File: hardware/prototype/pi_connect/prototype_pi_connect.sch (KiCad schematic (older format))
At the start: 29 parts, among them CON1 BARREL_JACK, SW1 Switch_SPDT_x2, SW2 Switch_SPDT_x2, U1 MCP23017, U2 Pi2_Connector, U3 MAX7221, U4 MAX7221

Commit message: Assign footprints
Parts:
- removed SW1, SW2: Switch_SPDT_x2, symbol Switch_SPDT_x2
- added SW1, SW2, SW3, SW4: SWITCH_INV, Buttons_Switches_ThroughHole:SW_Micro_SPST, symbol SWITCH_INV
- C1, C3: footprint (none) -> Discret:CP5
- C2, C4: footprint (none) -> Capacitors_ThroughHole:C_Disc_D6_P5
- CON1: footprint (none) -> Connect:BARREL_JACK
- D1, D10, D11, D12, D13, D14, D15, D16, D2, D3, D4, D5, D6, D7, D8, D9: footprint (none) -> LEDs:LED-5MM
- R1, R2: footprint (none) -> Resistors_ThroughHole:Resistor_Horizontal_RM10mm
- U1: footprint MODULE -> DIL28:DIL28
- U2: footprint MODULE -> CONN_02x20:CONN_02x20
- U3, U4: footprint MODULE -> DIL24:DIL24
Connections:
- net A_GPB0: now also SW4.3
- net A_GPB1: now also SW4.1
- net A_GPB2: now also SW3.3
- net A_GPB3: now also SW3.1
- net A_GPB4: now also SW2.3
- net A_GPB5: now also SW2.1
- net A_GPB6: now also SW1.3
- net A_GPB7: now also SW1.1
- net GND: now also SW1.2, SW2.2, SW3.2, SW4.2
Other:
- moved on the sheet: D1, D10, D11, D12, D13, D14, D15, D16, D2, D3, D4, D5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

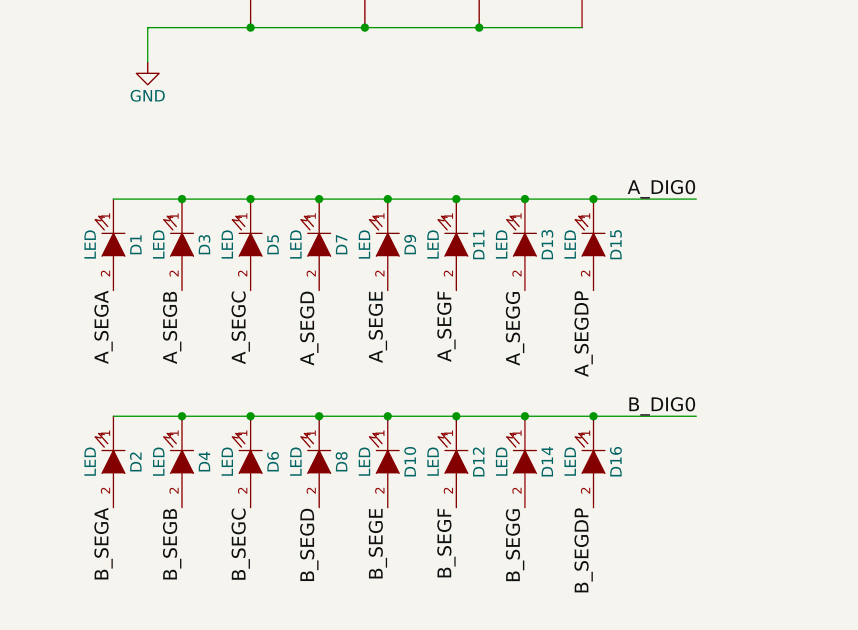
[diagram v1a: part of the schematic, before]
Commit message: Add footprint fot SPDT switches according to datasheet for 100SP4T1B1M2QEH. Also attempted to route some of this complex circuit manually.
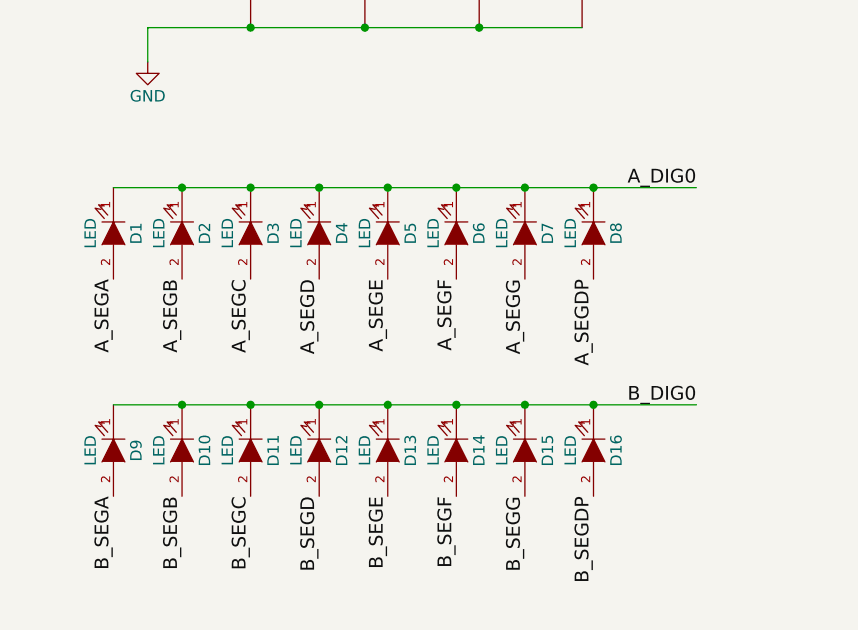
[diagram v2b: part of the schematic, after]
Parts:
- SW1, SW2, SW3, SW4: footprint Buttons_Switches_ThroughHole:SW_Micro_SPST -> myparts:SW_SPDT
- renumbered D4 to D10, D6 to D11, D8 to D12, D10 to D13, D12 to D14, D14 to D15, D3 to D2, D5 to D3, D7 to D4, D9 to D5, D11 to D6, D13 to D7, D15 to D8, D2 to D9
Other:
- moved on the sheet: D1, D10, D11, D12, D13, D14, D15, D16, D2, D3, D4, D5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
